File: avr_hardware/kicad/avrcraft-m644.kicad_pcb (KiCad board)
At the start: 2 copper layers, 85.1 x 49.8 mm, 49 parts, among them IC1 ATMEGA1284P-A, J1 AVRISP6, P1 ETHERNET, P10 PWR, P11 +5V, P12 GND, P13 GND, P14 PWR, P15 GND, P16 GND, P2 PWM, P3 I2C, P4 GND, P5 SERIAL, P6 DIO, P7 3V3, P8 AIO, P9 AIO, T1 S558-5999-T7-F, U1 RN-150, U10 LSM303C, U11 CN-100n, U2 MCP1824v3.3, U3 ENC424J600, U4 RN-150, U5 RN-1k, U6 CN-10n, U7 RN-49.9, U8 RN-1k, U9 AP1117v5.0, X1 20MHz, X2 25MHz

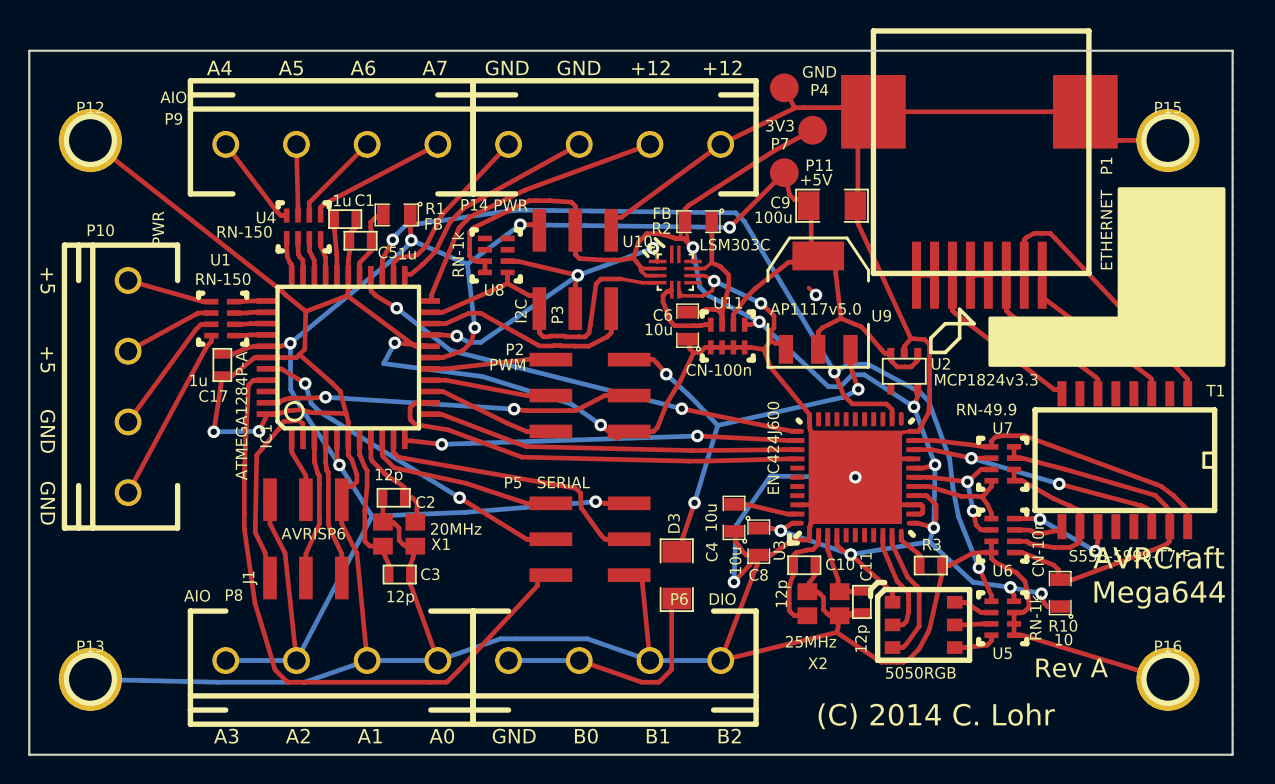
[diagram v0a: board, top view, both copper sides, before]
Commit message: Update for use with dedicated serial port.
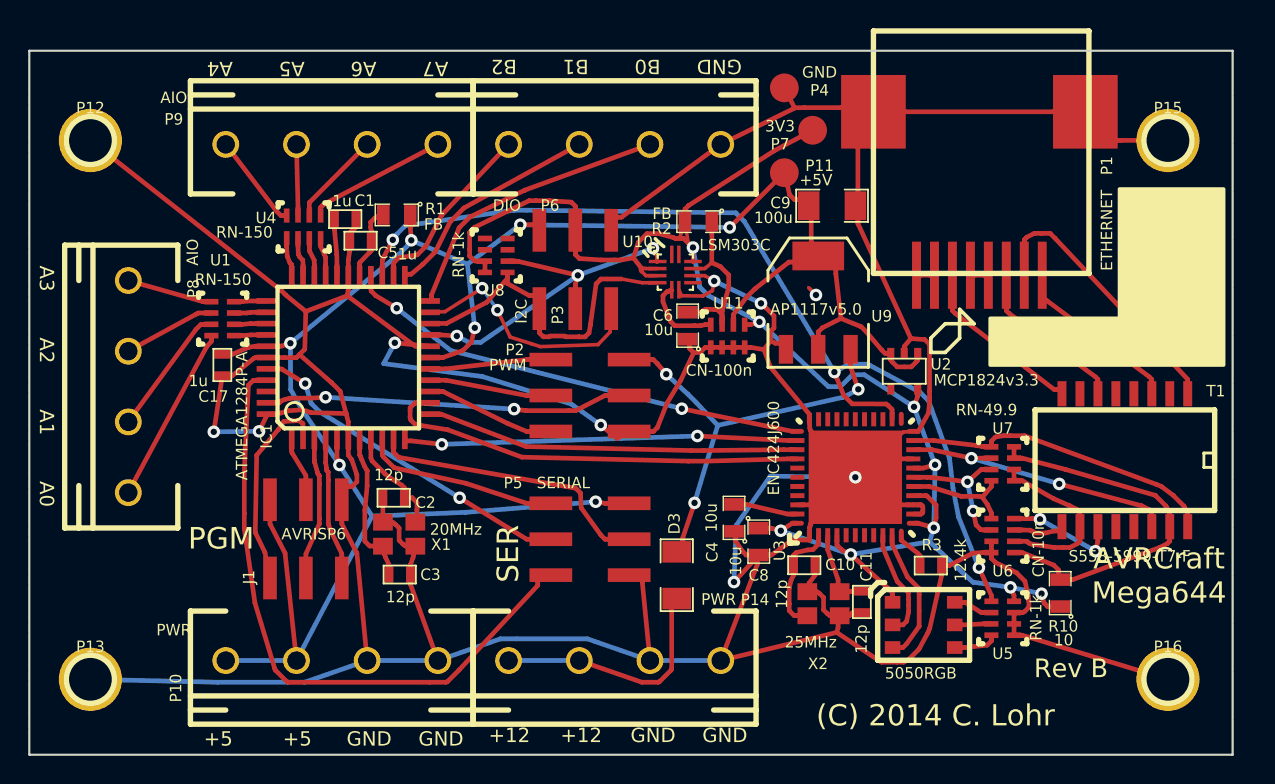
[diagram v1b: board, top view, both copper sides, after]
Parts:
- moved P14 36.5 mm to (96.0, 130.5), turned to 0 degrees
- moved P6 36.5 mm to (96.0, 94.0), turned to 180 degrees
- moved P10 24.1 mm to (76.0, 130.5), turned to 0 degrees
- moved P8 24.1 mm to (61.6, 111.1), turned to 270 degrees
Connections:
- D3 pad 1: N-0000054 (its old number) -> N-0000032
- IC1 pad 19: N-0000045 (its old number) -> /SCL
- IC1 pad 20: N-0000013 (its old number) -> /SDA
- IC1 pad 21: N-0000047 (its old number) -> N-0000079
- IC1 pad 22: N-0000056 (its old number) -> N-0000031
- IC1 pad 23: N-0000057 (its old number) -> N-0000030
- IC1 pad 24: N-0000058 (its old number) -> N-0000029
- IC1 pad 42: N-0000079 -> (no net)
- P10 pad 1: N-0000019 (its old number) -> +5V
- P10 pad 2: N-0000020 (its old number) -> +5V
- P10 pad 3: N-0000021 (its old number) -> GND
- P10 pad 4: N-0000014 (its old number) -> GND
- P14 pad 1: GND -> N-0000032
- P14 pad 2: N-0000056 (its old number) -> N-0000032
- P14 pad 3: N-0000057 (its old number) -> GND
- P14 pad 4: N-0000058 (its old number) -> GND
- P3 pad 1: N-0000047 (its old number) -> /SDA
- P3 pad 3: N-0000045 (its old number) -> /SCL
- P3 pad 5: N-0000013 (its old number) -> N-0000079
- P6 pad 1: N-0000054 (its old number) -> GND
- P6 pad 2: N-0000054 (its old number) -> N-0000031
- P6 pad 3: GND -> N-0000030
- P6 pad 4: GND -> N-0000029
- P8 pad 1: +5V -> N-0000011
- P8 pad 2: +5V -> N-0000010
- P8 pad 3: GND -> N-000009
- P8 pad 4: GND -> N-000008
- T1 pad 12: N-0000097 (its old number) -> (no net)
- T1 pad 13: N-0000098 -> (no net)
- T1 pad 2: N-0000085 (its old number) -> (no net)
- T1 pad 4: N-0000086 -> (no net)
- T1 pad 5: N-0000087 (its old number) -> (no net)
- T1 pad 7: N-0000089 -> (no net)
- U1 pad 5: N-0000019 (its old number) -> N-0000011
- U1 pad 6: N-0000020 (its old number) -> N-0000010
- U1 pad 7: N-0000021 (its old number) -> N-000009
- U1 pad 8: N-0000014 (its old number) -> N-000008
- U10 pad 1: N-0000045 (its old number) -> /SCL
- U10 pad 11: N-0000036 (its old number) -> (no net)
- U10 pad 12: N-0000037 (its old number) -> (no net)
- U10 pad 4: N-0000047 (its old number) -> /SDA
- U10 pad 7: N-0000035 (its old number) -> (no net)
- U2 pad 4: N-0000093 -> (no net)
- U3 pad 23: N-0000075 -> (no net)
- U3 pad 25: N-0000077 -> (no net)
- U3 pad 26: N-0000065 -> (no net)
- U3 pad 27: N-0000060 -> (no net)
- U3 pad 28: N-0000061 (its old number) -> (no net)
- U3 pad 29: N-0000063 (its old number) -> (no net)
- U3 pad 30: N-0000069 -> (no net)
- U3 pad 31: N-0000072 -> (no net)
- U3 pad 32: N-0000074 -> (no net)
- U3 pad 38: N-0000062 (its old number) -> (no net)
- U3 pad 39: N-0000064 (its old number) -> (no net)
- U3 pad 40: N-0000070 -> (no net)
- U3 pad 41: N-0000073 -> (no net)
- U3 pad 5: N-0000095 (its old number) -> (no net)
- U3 pad 6: N-0000096 -> (no net)
- U3 pad 7: N-0000080 -> (no net)
- U3 pad 8: N-0000066 -> (no net)
- U8 pad 1: N-0000047 (its old number) -> /SDA
- U8 pad 2: N-0000045 (its old number) -> /SCL
- U8 pad 3: N-00000102 -> (no net)
- U8 pad 4: N-00000103 -> (no net)
- U8 pad 5: N-00000104 -> (no net)
- U8 pad 6: N-00000105 -> (no net)
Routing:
- net N-0000045 (its old number): track 26.3 -> 0.00 mm, vias 3 -> 0
- net /SCL: track 0.00 -> 26.3 mm, vias 0 -> 3
- net /SDA: track 0.00 -> 24.1 mm
- net N-0000047 (its old number): track 23.4 -> 0.00 mm
- net N-0000056 (its old number): track 20.5 -> 0.00 mm
- net N-0000031: track 0.00 -> 20.5 mm
- net N-0000079: track 0.00 -> 17.4 mm, vias 0 -> 2
- net N-0000054 (its old number): track 17.3 -> 0.00 mm
- net N-0000032: track 0.00 -> 17.3 mm
- net N-0000030: track 0.00 -> 16.0 mm
- net N-0000057 (its old number): track 16.0 -> 0.00 mm
- net N-0000013 (its old number): track 15.6 -> 0.00 mm
- net N-0000058 (its old number): track 13.0 -> 0.00 mm
- net N-0000029: track 0.00 -> 13.0 mm
- net N-000008: track 0.00 -> 12.6 mm
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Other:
- board text added: "PGM"
- board text added: "Rev B"
- board text added: "SER"
- board text removed: "Rev A"
